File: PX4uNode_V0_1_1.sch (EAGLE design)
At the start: 129 parts, among them M3_MOUNT1101 MOUNT-HOLE3.1MM, M3_MOUNT1102 MOUNT-HOLE3.1MM, M3_MOUNT1103 MOUNT-HOLE3.1MM, M3_MOUNT1104 MOUNT-HOLE3.1MM, U101 STM32F4X7VX, U401 MAX3051, U402 MAX3051, X101 3.2x2.5 mm / 24 MHz / 15 ppm

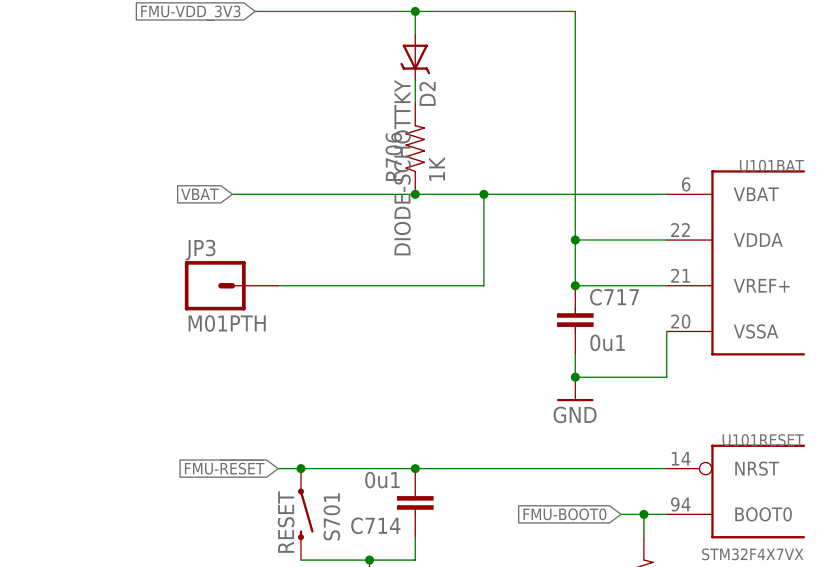
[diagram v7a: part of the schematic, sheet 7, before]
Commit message: Battery added.  Floods added to power tracks
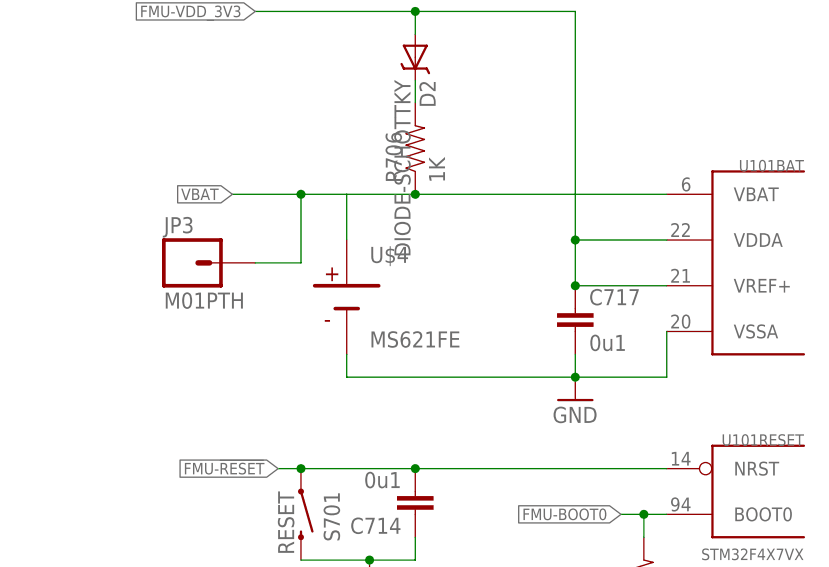
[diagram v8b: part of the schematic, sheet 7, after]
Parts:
- added U$4: MS621FE, pixhawk2:MS621FE
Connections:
- net GND: now also U$4.NEG
- net VBAT: now also U$4.POS
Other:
- moved on the sheet: JP3
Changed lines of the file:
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@@
 <attribute name="PARTNO" value="RC0402FR-0710KL"/>
 </part>
+<part name="U$4" library="pixhawk2" deviceset="MS621FE" device=""/>
 </parts>
 <sheets>
@@
 <attribute name="PARTNO" x="139.7" y="50.8" size="1.778" layer="96" rot="R90" display="off"/>
 </instance>
-<instance part="JP3" gate="G$1" x="182.88" y="101.6"/>
+<instance part="JP3" gate="G$1" x="180.34" y="104.14"/>
+<instance part="U$4" gate="G$1" x="198.12" y="101.6"/>
 </instances>
 <busses>
@@
 <wire x1="233.68" y1="91.44" x2="233.68" y2="96.52" width="0.1524" layer="91"/>
 <junction x="223.52" y="91.44"/>
+<pinref part="U$4" gate="G$1" pin="NEG"/>
+<wire x1="198.12" y1="93.98" x2="198.12" y2="91.44" width="0.1524" layer="91"/>
+<wire x1="198.12" y1="91.44" x2="223.52" y2="91.44" width="0.1524" layer="91"/>
 </segment>
 <segment>
@@
 <segment>
 <pinref part="U101" gate="BAT" pin="VBAT"/>
-<wire x1="205.74" y1="111.76" x2="213.36" y2="111.76" width="0.1524" layer="91"/>
 <junction x="205.74" y="111.76"/>
-<wire x1="213.36" y1="111.76" x2="233.68" y2="111.76" width="0.1524" layer="91"/>
-<wire x1="205.74" y1="111.76" x2="185.42" y2="111.76" width="0.1524" layer="91"/>
+<wire x1="205.74" y1="111.76" x2="233.68" y2="111.76" width="0.1524" layer="91"/>
+<wire x1="205.74" y1="111.76" x2="198.12" y2="111.76" width="0.1524" layer="91"/>
 <label x="185.42" y="111.76" size="1.27" layer="95" rot="R180" xref="yes"/>
 <pinref part="R706" gate="G$1" pin="1"/>
-<junction x="213.36" y="111.76"/>
+<junction x="193.04" y="111.76"/>
 <pinref part="JP3" gate="G$1" pin="1"/>
-<wire x1="190.5" y1="101.6" x2="213.36" y2="101.6" width="0.1524" layer="91"/>
-<wire x1="213.36" y1="101.6" x2="213.36" y2="111.76" width="0.1524" layer="91"/>
-</segment>
-</net>
+<wire x1="198.12" y1="111.76" x2="193.04" y2="111.76" width="0.1524" layer="91"/>
+<wire x1="193.04" y1="111.76" x2="185.42" y2="111.76" width="0.1524" layer="91"/>
+<wire x1="187.96" y1="104.14" x2="193.04" y2="104.14" width="0.1524" layer="91"/>
+<wire x1="193.04" y1="104.14" x2="193.04" y2="111.76" width="0.1524" layer="91"/>
+<pinref part="U$4" gate="G$1" pin="POS"/>
+<wire x1="198.12" y1="106.68" x2="198.12" y2="111.76" width="0.1524" layer="91"/>
+</segment>
+</net>
